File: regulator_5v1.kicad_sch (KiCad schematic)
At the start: 14 parts

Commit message: sorry can ignore if u want
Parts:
- U6: value ~ -> AP64501SP-13
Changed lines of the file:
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@@
 			)
 		)
-		(property "Value" "~"
+		(property "Value" "AP64501SP-13"
 			(at 105.41 62.23 0)
 			(effects

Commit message: 5.1
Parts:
- removed C45: C, symbol Device:C
- C42: value C -> 10uF
- C43: value C -> 10nF
- C44: value C -> 100nF
- C46: value C -> 2.7nF
- C47: value C -> 47pF
- C48, C49, C50: value C -> 22uF
- L4: value L -> 3.6uF
- R18: value R -> 16k
- R19: value R -> 118k
- R20: value R -> 22.1k
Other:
- moved on the sheet: C47, C50
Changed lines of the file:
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@@
 	)
 	(junction
-		(at 137.16 69.85)
+		(at 135.89 69.85)
 		(diameter 0)
 		(color 0 0 0 0)
@@
 	)
 	(junction
-		(at 125.73 91.44)
-		(diameter 0)
-		(color 0 0 0 0)
-	)
-	(junction
 		(at 91.44 67.31)
 		(diameter 0)
@@
 	)
 	(junction
+		(at 135.89 77.47)
+		(diameter 0)
+		(color 0 0 0 0)
+	)
+	(junction
 		(at 147.32 77.47)
 		(diameter 0)
@@
 	)
 	(junction
-		(at 116.84 74.93)
-		(diameter 0)
-		(color 0 0 0 0)
-	)
-	(junction
 		(at 87.63 91.44)
 		(diameter 0)
@@
 	)
 	(junction
-		(at 137.16 77.47)
-		(diameter 0)
-		(color 0 0 0 0)
-	)
-	(junction
 		(at 147.32 69.85)
 		(diameter 0)
@@
 	(wire
 		(pts
-			(xy 132.08 77.47) (xy 137.16 77.47)
+			(xy 127 77.47) (xy 135.89 77.47)
 		)
 		(stroke
@@
 	(wire
 		(pts
-			(xy 114.3 72.39) (xy 132.08 72.39)
+			(xy 114.3 72.39) (xy 127 72.39)
 		)
 		(stroke
@@
 	(wire
 		(pts
-			(xy 125.73 77.47) (xy 125.73 74.93)
-		)
-		(stroke
-			(width 0)
-			(type default)
-		)
-	)
-	(wire
-		(pts
-			(xy 125.73 91.44) (xy 116.84 91.44)
+			(xy 116.84 91.44) (xy 147.32 91.44)
 		)
 		(stroke
@@
 	(wire
 		(pts
-			(xy 147.32 91.44) (xy 125.73 91.44)
-		)
-		(stroke
-			(width 0)
-			(type default)
-		)
-	)
-	(wire
-		(pts
-			(xy 134.62 69.85) (xy 137.16 69.85)
-		)
-		(stroke
-			(width 0)
-			(type default)
-		)
-	)
-	(wire
-		(pts
-			(xy 168.91 69.85) (xy 179.07 69.85)
-		)
-		(stroke
-			(width 0)
-			(type default)
-		)
-	)
-	(wire
-		(pts
-			(xy 132.08 72.39) (xy 132.08 77.47)
+			(xy 134.62 69.85) (xy 135.89 69.85)
+		)
+		(stroke
+			(width 0)
+			(type default)
+		)
+	)
+	(wire
+		(pts
+			(xy 168.91 69.85) (xy 180.34 69.85)
+		)
+		(stroke
+			(width 0)
+			(type default)
+		)
+	)
+	(wire
+		(pts
+			(xy 127 72.39) (xy 127 77.47)
 		)
 		(stroke
@@
 	(wire
 		(pts
-			(xy 168.91 91.44) (xy 179.07 91.44)
-		)
-		(stroke
-			(width 0)
-			(type default)
-		)
-	)
-	(wire
-		(pts
-			(xy 125.73 74.93) (xy 116.84 74.93)
+			(xy 135.89 77.47) (xy 147.32 77.47)
+		)
+		(stroke
+			(width 0)
+			(type default)
+		)
+	)
+	(wire
+		(pts
+			(xy 168.91 91.44) (xy 180.34 91.44)
 		)
 		(stroke
@@
 	(wire
 		(pts
-			(xy 137.16 77.47) (xy 147.32 77.47)
-		)
-		(stroke
-			(width 0)
-			(type default)
-		)
-	)
-	(wire
-		(pts
 			(xy 157.48 69.85) (xy 168.91 69.85)
 		)
@@
 	(wire
 		(pts
-			(xy 179.07 91.44) (xy 179.07 77.47)
-		)
-		(stroke
-			(width 0)
-			(type default)
-		)
-	)
-	(wire
-		(pts
-			(xy 137.16 69.85) (xy 147.32 69.85)
-		)
-		(stroke
-			(width 0)
-			(type default)
-		)
-	)
-	(wire
-		(pts
-			(xy 125.73 85.09) (xy 125.73 91.44)
+			(xy 180.34 91.44) (xy 180.34 77.47)
+		)
+		(stroke
+			(width 0)
+			(type default)
+		)
+	)
+	(wire
+		(pts
+			(xy 135.89 69.85) (xy 147.32 69.85)
 		)
 		(stroke
@@
 			)
 		)
-		(property "Value" "R"
+		(property "Value" "22.1k"
 			(at 149.86 85.0899 0)
 			(effects
@@
 			)
 		)
-		(property "Value" "R"
+		(property "Value" "118k"
 			(at 149.86 74.9299 0)
 			(effects
@@
 	(symbol
 		(lib_id "Device:C")
-		(at 137.16 73.66 0)
+		(at 135.89 73.66 0)
 		(unit 1)
 		(exclude_from_sim no)
@@
 		(fields_autoplaced yes)
 		(property "Reference" "C47"
-			(at 140.97 72.3899 0)
-			(effects
-				(font
-					(size 1.27 1.27)
-				)
-				(justify left)
-			)
-		)
-		(property "Value" "C"
-			(at 140.97 74.9299 0)
+			(at 139.7 72.3899 0)
+			(effects
+				(font
+					(size 1.27 1.27)
+				)
+				(justify left)
+			)
+		)
+		(property "Value" "47pF"
+			(at 139.7 74.9299 0)
 			(effects
 				(font
@@
 		)
 		(property "Footprint" ""
-			(at 138.1252 77.47 0)
+			(at 136.8552 77.47 0)
 			(effects
 				(font
@@
 		)
 		(property "Datasheet" "~"
-			(at 137.16 73.66 0)
+			(at 135.89 73.66 0)
 			(effects
 				(font
@@
 		)
 		(property "Description" "Unpolarized capacitor"
-			(at 137.16 73.66 0)
+			(at 135.89 73.66 0)
 			(effects
 				(font
@@
 			)
 		)
-		(property "Value" "C"
+		(property "Value" "22uF"
 			(at 161.29 74.9299 0)
 			(effects
@@
 			)
 		)
-		(property "Value" "C"
+		(property "Value" "10uF"
 			(at 82.55 72.3899 0)
 			(effects
@@
 	(symbol
 		(lib_id "Device:C")
-		(at 179.07 73.66 0)
+		(at 180.34 73.66 0)
 		(unit 1)
 		(exclude_from_sim no)
@@
 		(fields_autoplaced yes)
 		(property "Reference" "C50"
-			(at 182.88 72.3899 0)
-			(effects
-				(font
-					(size 1.27 1.27)
-				)
-				(justify left)
-			)
-		)
-		(property "Value" "C"
-			(at 182.88 74.9299 0)
+			(at 184.15 72.3899 0)
+			(effects
+				(font
+					(size 1.27 1.27)
+				)
+				(justify left)
+			)
+		)
+		(property "Value" "22uF"
+			(at 184.15 74.9299 0)
 			(effects
 				(font
@@
 		)
 		(property "Footprint" ""
-			(at 180.0352 77.47 0)
+			(at 181.3052 77.47 0)
 			(effects
 				(font
@@
 		)
 		(property "Datasheet" "~"
-			(at 179.07 73.66 0)
+			(at 180.34 73.66 0)
 			(effects
 				(font
@@
 		)
 		(property "Description" "Unpolarized capacitor"
-			(at 179.07 73.66 0)
+			(at 180.34 73.66 0)
 			(effects
 				(font
@@
 			)
 		)
-		(property "Value" "L"
+		(property "Value" "3.6uF"
 			(at 130.81 67.31 90)
 			(effects
@@
 			)
 		)
-		(property "Value" "C"
+		(property "Value" "2.7nF"
 			(at 120.65 87.6299 0)
 			(effects
@@
 			)
 		)
-		(property "Value" "R"
+		(property "Value" "16k"
 			(at 119.38 80.0099 0)
 			(effects
@@
 			)
 		)
-		(property "Value" "C"
+		(property "Value" "100nF"
 			(at 121.92 62.23 90)
 			(effects
@@
 			)
 		)
-		(property "Value" "C"
+		(property "Value" "10nF"
 			(at 91.44 82.5499 0)
 			(effects
@@
 			)
 		)
-		(property "Value" "C"
+		(property "Value" "22uF"
 			(at 172.72 74.9299 0)
 			(effects
@@
 					(unit 1)
 				)
-			)
-		)
-	)
-	(symbol
-		(lib_id "Device:C")
-		(at 125.73 81.28 0)
-		(unit 1)
-		(exclude_from_sim no)
-		(in_bom yes)
-		(on_board yes)
-		(dnp no)
-		(fields_autoplaced yes)
-		(property "Reference" "C45"
-			(at 129.54 80.0099 0)
-			(effects
-				(font
-					(size 1.27 1.27)
-				)
-				(justify left)
-			)
-		)
-		(property "Value" "C"
-			(at 129.54 82.5499 0)
-			(effects
-				(font
-					(size 1.27 1.27)
-				)
-				(justify left)
-			)
-		)
-		(property "Footprint" ""
-			(at 126.6952 85.09 0)
-			(effects
-				(font
-					(size 1.27 1.27)
-				)
-				(hide yes)
-			)
-		)
-		(property "Datasheet" "~"
-			(at 125.73 81.28 0)
-			(effects
-				(font
-					(size 1.27 1.27)
-				)
-				(hide yes)
-			)
-		)
-		(property "Description" "Unpolarized capacitor"
-			(at 125.73 81.28 0)
-			(effects
-				(font
-					(size 1.27 1.27)
-				)
-				(hide yes)
-			)
-		)
-		(pin "2"
-		)
-		(pin "1"
-		)
-		(instances
-			(project ""
-				(path "/2f56b371-1597-47e1-a48d-b7f69d342f77/eed5055e-310e-40b9-8812-77db8a815e44"
-					(reference "C45")
-					(unit 1)
-				)

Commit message: all one component?
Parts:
- added C17, C45, C61: 10uF, symbol Device:C
- added C18, C51, C62: 10nF, symbol Device:C
- added C39, C52, C63: 2.7nF, symbol Device:C
- added C40, C53, C64: 100nF, symbol Device:C
- added C41, C54, C65: 47pF, symbol Device:C
- added C55, C56, C57, C58, C59, C60, C66, C67, C68: 22uF, symbol Device:C
- added L2: 3.6uH, symbol Device:L
- added L3: 10uH, symbol Device:L
- added L5: 3.3uH, symbol Device:L
- added R21: 10.5k, symbol Device:R
- added R22: 69.8k, symbol Device:R
- added R23: 22.1k, symbol Device:R
- added R24: 15.8k, symbol Device:R
- added R25: 115.8k, symbol Device:R
- added R26, R29: 22.1, symbol Device:R
- added R27: 37.4, symbol Device:R
- added R28: 309.0, symbol Device:R
- added U3, U5, U7: AP64501SP-13, Package_SO:SOIC-8-1EP_3.9x4.9mm_P1.27mm_EP2.29x3mm, symbol Regulator_Switching:AP64501SP-13
- L4: value 3.6uF -> 3.6uH
- U6: footprint (none) -> Package_SO:SOIC-8-1EP_3.9x4.9mm_P1.27mm_EP2.29x3mm
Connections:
- net GND: now also C17.2, C18.2, C39.2, C45.2, C51.2, C52.2, C55.2, C56.2, C57.2, C58.2, C59.2, C60.2, C61.2, C62.2, C63.2, C66.2, C67.2, C68.2, R23.2, R26.2, R29.2, U3.7 (GND), U5.7 (GND), U7.7 (GND)
- new net: C40.1, U3.1 (BST)
- new net: C40.2, L2.1, U3.8 (SW)
- new net: C54.1, C55.1, C56.1, C57.1, L5.2, R22.1
- new net: R27.1, U5.6 (COMP)
- new net: C63.1, R27.2
- new net: C53.2, L5.1, U7.8 (SW)
- new net: C65.1, C66.1, C67.1, C68.1, L3.2, R28.1
- new net: C17.1, U3.2 (VIN), U3.3 (EN)
- new net: R24.1, U3.6 (COMP)
- new net: C39.1, R24.2
- new net: C41.2, R25.2, R26.1, U3.5 (FB)
- new net: C41.1, C58.1, C59.1, C60.1, L2.2, R25.1
- new net: C45.1, U7.2 (VIN), U7.3 (EN)
- new net: C18.1, U3.4 (SS)
- new net: C53.1, U7.1 (BST)
- new net: C65.2, R28.2, R29.1, U5.5 (FB)
- new net: C54.2, R22.2, R23.1, U7.5 (FB)
- new net: C51.1, U7.4 (SS)
- new net: C61.1, U5.2 (VIN), U5.3 (EN)
- new net: C64.2, L3.1, U5.8 (SW)
- new net: C64.1, U5.1 (BST)
- new net: C62.1, U5.4 (SS)
- new net: R21.1, U7.6 (COMP)
- new net: C52.1, R21.2
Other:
- note added: "12V"
- note added: "3V3"
- note added: "5.1V"
- note added: "5V"
- moved on the sheet: C42, C43, C44, C46, C47, C48, C49, C50, L4, R18, R19, R20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

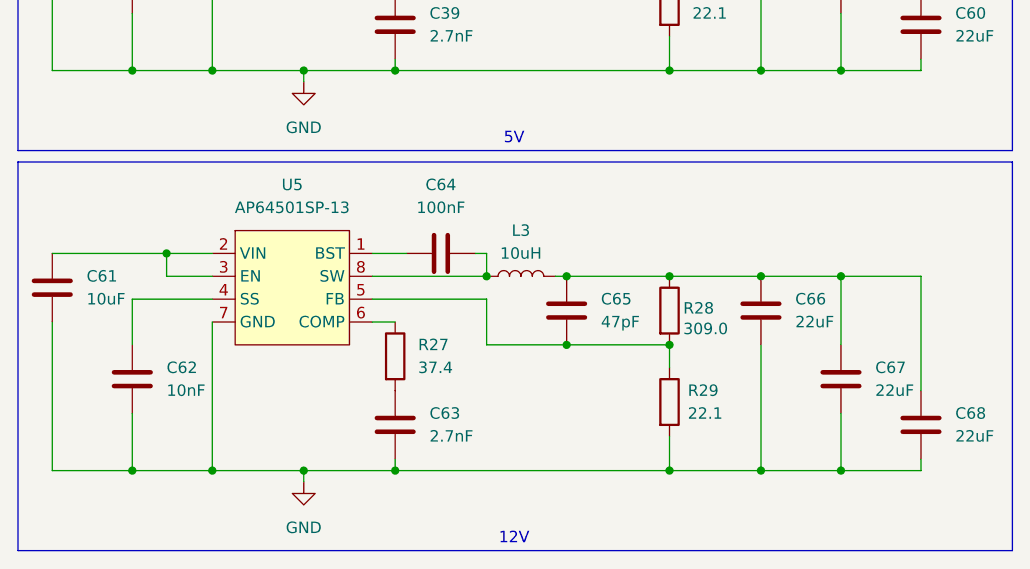
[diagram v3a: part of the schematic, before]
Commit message: remove 12V
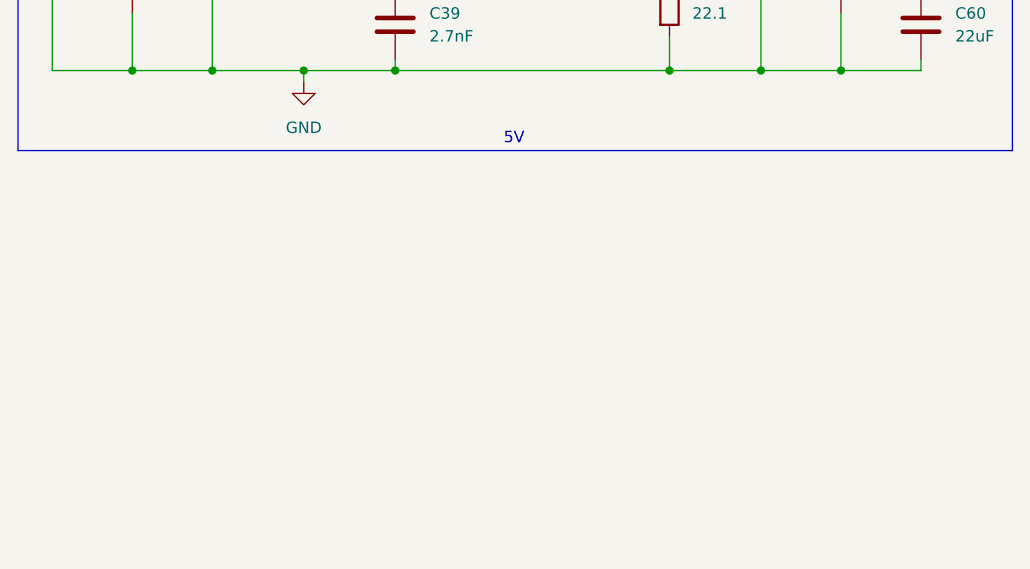
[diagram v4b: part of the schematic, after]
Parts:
- removed C61: 10uF, symbol Device:C
- removed C62: 10nF, symbol Device:C
- removed C63: 2.7nF, symbol Device:C
- removed C64: 100nF, symbol Device:C
- removed C65: 47pF, symbol Device:C
- removed C66, C67, C68: 22uF, symbol Device:C
- removed L3: 10uH, symbol Device:L
- removed R27: 37.4, symbol Device:R
- removed R28: 309.0, symbol Device:R
- removed R29: 22.1, symbol Device:R
- removed U5: AP64501SP-13, Package_SO:SOIC-8-1EP_3.9x4.9mm_P1.27mm_EP2.29x3mm, symbol Regulator_Switching:AP64501SP-13
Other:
- note removed: "12V"
